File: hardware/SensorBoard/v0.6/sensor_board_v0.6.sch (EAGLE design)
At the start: 48 parts, among them J3 USB-MICROB, U1 ATMEGA328P, U10 CCS811, U11 RFM69HW, U2 TSL2561, U4 MPL115A, U5 FT231XS, U7 SHT31, U8 MCP1703/3.3V, U9 MCP1703CB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

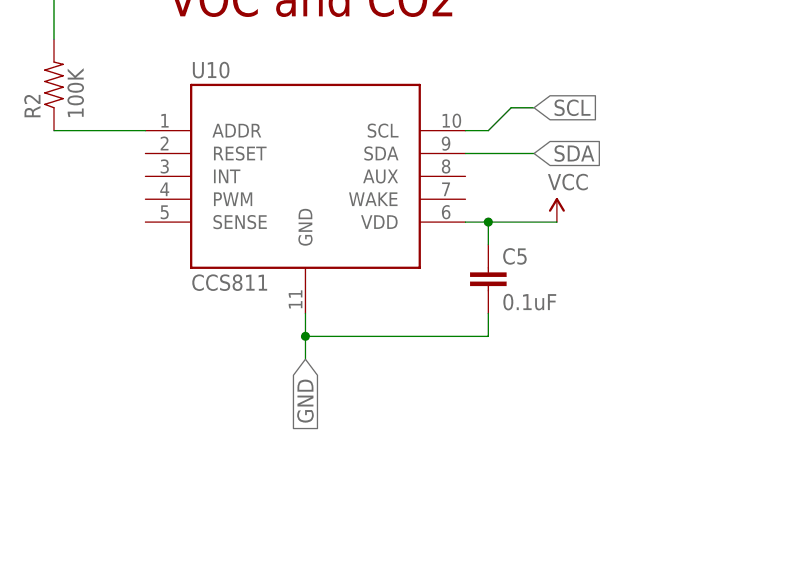
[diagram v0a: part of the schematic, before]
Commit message: Minor fixes to sensor board v0.6
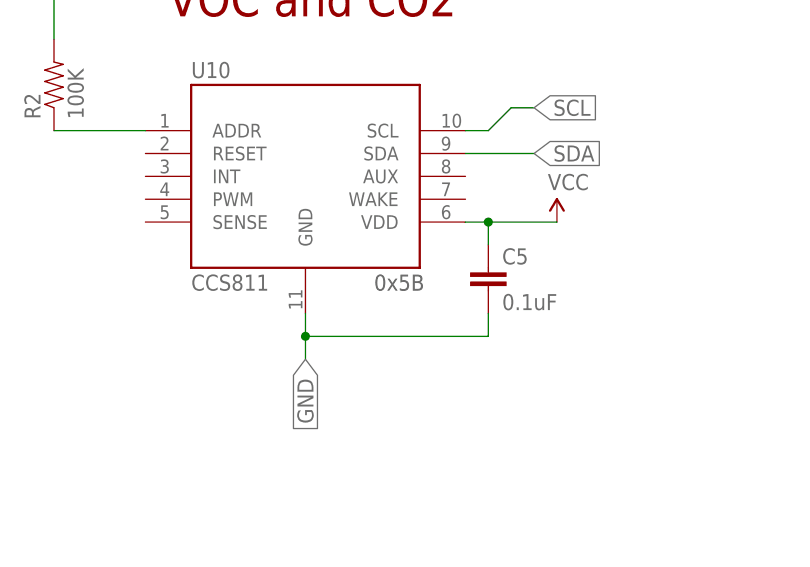
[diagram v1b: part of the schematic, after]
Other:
- note added: "0x5B"
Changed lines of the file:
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@@
 <text x="157.48" y="17.78" size="1.778" layer="97">0x60</text>
 <text x="309.88" y="-22.86" size="1.778" layer="97">0x44</text>
+<text x="182.88" y="88.9" size="1.778" layer="97">0x5B</text>
 </plain>
 <instances>
